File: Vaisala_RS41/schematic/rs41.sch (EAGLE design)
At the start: 268 parts, among them J201 SENSORBOOM, J601 expansion, J602 XDATA, Q201 BSS92, Q202 BSS92, Q203 BSS101, Q204 BSS101, Q501 E4JxA, Q502 BSS101, Q503 BSS101, Q601 BSS101, U101 STM32F100C8T6B, U201 TS3A4751, U202 TS5A9411, U203 TS5A9411, U204 TS5A9411, U205 74HCU04, U206 305G, U207 74LVC3G34, U208 NC7SZ27, U301 DIFFGEN, U302 UBX-6010MLF56, U303 SAW, U304 LNA, U401 SI4032QFN204X4, U501 TLV70030SOT23-5, U502 TPS61200, U503 TLV70030SOT23-5, U504 TLV70030SOT23-5, U601 25AA080SN, X101 24MHz, X301 tbd

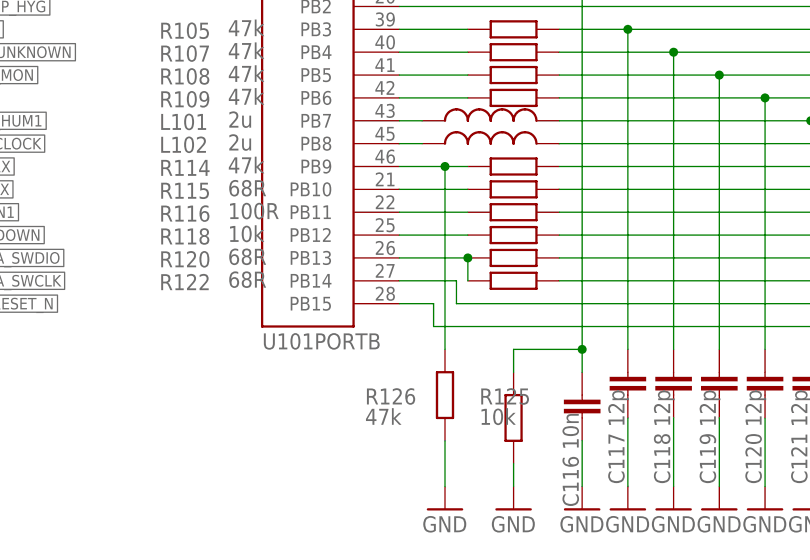
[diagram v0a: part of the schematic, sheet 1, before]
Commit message: R125 in RS41 sonde is connected to +3V, not GND, fixed
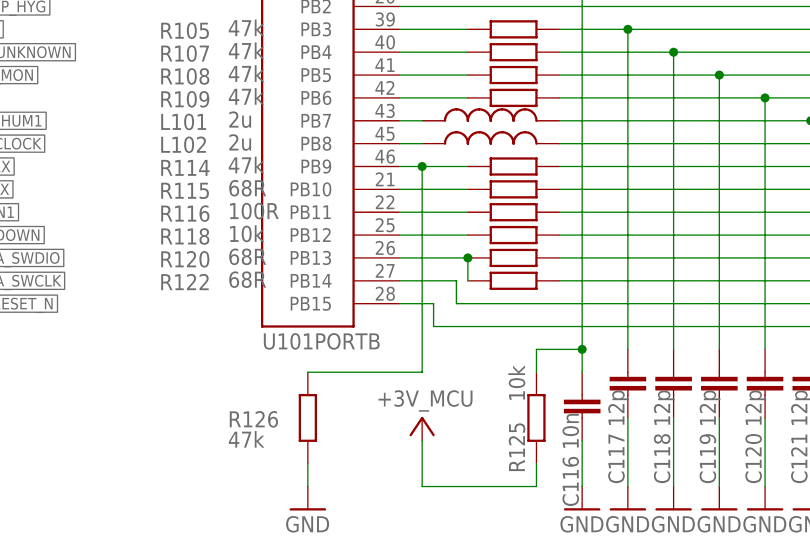
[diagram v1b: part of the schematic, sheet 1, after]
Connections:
- net +3V_MCU: now also R125.2
- net GND: no longer R125.2
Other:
- moved on the sheet: R125, R126
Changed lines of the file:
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@@
 <part name="GND4" library="supply1" library_urn="urn:adsk.eagle:library:371" deviceset="GND" device=""/>
 <part name="P+2" library="rs41" deviceset="+3V_ANA" device=""/>
-<part name="GND5" library="supply1" library_urn="urn:adsk.eagle:library:371" deviceset="GND" device=""/>
 <part name="F501" library="rs41" deviceset="FUSE" device="" value="tbd"/>
 <part name="GND6" library="supply1" library_urn="urn:adsk.eagle:library:371" deviceset="GND" device=""/>
@@
 <part name="P+11" library="rs41" deviceset="+3V_GPS" device=""/>
 <part name="GND20" library="supply1" library_urn="urn:adsk.eagle:library:371" deviceset="GND" device=""/>
+<part name="P+12" library="rs41" deviceset="+3V_MCU" device=""/>
 </parts>
 <sheets>
@@
 <attribute name="VALUE" x="-17.78" y="-20.32" size="1.778" layer="96"/>
 </instance>
-<instance part="R125" gate="G$1" x="66.04" y="-7.62" smashed="yes" rot="R270">
-<attribute name="NAME" x="62.23" y="-6.1214" size="1.778" layer="95"/>
-<attribute name="VALUE" x="62.23" y="-8.382" size="1.778" layer="96"/>
-</instance>
-<instance part="R126" gate="G$1" x="58.42" y="-5.08" smashed="yes" rot="R270">
-<attribute name="NAME" x="49.53" y="-6.1214" size="1.778" layer="95"/>
-<attribute name="VALUE" x="49.53" y="-8.382" size="1.778" layer="96"/>
+<instance part="R125" gate="G$1" x="68.58" y="-7.62" smashed="yes" rot="R270">
+<attribute name="NAME" x="67.31" y="-13.7414" size="1.778" layer="95" rot="R90"/>
+<attribute name="VALUE" x="67.31" y="-5.842" size="1.778" layer="96" rot="R90"/>
+</instance>
+<instance part="R126" gate="G$1" x="43.18" y="-7.62" smashed="yes" rot="R270">
+<attribute name="NAME" x="34.29" y="-8.6614" size="1.778" layer="95"/>
+<attribute name="VALUE" x="34.29" y="-10.922" size="1.778" layer="96"/>
 </instance>
 <instance part="C117" gate="G$1" x="78.74" y="-5.08" smashed="yes" rot="R180">
@@
 <attribute name="VALUE" x="34.29" y="6.858" size="1.778" layer="96"/>
 </instance>
-<instance part="GND114" gate="1" x="58.42" y="-17.78" smashed="yes">
-<attribute name="VALUE" x="55.88" y="-20.32" size="1.778" layer="96"/>
+<instance part="GND114" gate="1" x="43.18" y="-17.78" smashed="yes">
+<attribute name="VALUE" x="40.64" y="-20.32" size="1.778" layer="96"/>
 </instance>
 <instance part="GND115" gate="1" x="73.66" y="-17.78" smashed="yes">
@@
 <attribute name="VALUE" x="2.54" y="60.96" size="1.778" layer="96"/>
 </instance>
-<instance part="GND5" gate="1" x="66.04" y="-17.78" smashed="yes">
-<attribute name="VALUE" x="63.5" y="-20.32" size="1.778" layer="96"/>
-</instance>
 <instance part="L101" gate="G$1" x="63.5" y="25.4" smashed="yes" rot="R90">
 <attribute name="NAME" x="26.67" y="24.384" size="1.778" layer="95"/>
@@
 <attribute name="NAME" x="26.67" y="21.844" size="1.778" layer="95"/>
 <attribute name="VALUE" x="34.29" y="22.098" size="1.778" layer="96"/>
+</instance>
+<instance part="P+12" gate="G$1" x="55.88" y="-7.62" smashed="yes">
+<attribute name="VALUE" x="50.8" y="-6.35" size="1.778" layer="96"/>
 </instance>
 </instances>
@@
 <pinref part="GND114" gate="1" pin="GND"/>
 <pinref part="R126" gate="G$1" pin="2"/>
-<wire x1="58.42" y1="-10.16" x2="58.42" y2="-15.24" width="0.1524" layer="91"/>
+<wire x1="43.18" y1="-12.7" x2="43.18" y2="-15.24" width="0.1524" layer="91"/>
 </segment>
 <segment>
@@
 <pinref part="GND3" gate="1" pin="GND"/>
 </segment>
-<segment>
-<pinref part="R125" gate="G$1" pin="2"/>
-<pinref part="GND5" gate="1" pin="GND"/>
-<wire x1="66.04" y1="-15.24" x2="66.04" y2="-12.7" width="0.1524" layer="91"/>
-</segment>
 </net>
 <net name="N$106" class="0">
@@
 <pinref part="R114" gate="G$1" pin="2"/>
 <pinref part="U101" gate="PORTB" pin="PB9"/>
-<wire x1="60.96" y1="20.32" x2="58.42" y2="20.32" width="0.1524" layer="91"/>
+<wire x1="60.96" y1="20.32" x2="55.88" y2="20.32" width="0.1524" layer="91"/>
 <pinref part="R126" gate="G$1" pin="1"/>
-<wire x1="58.42" y1="20.32" x2="53.34" y2="20.32" width="0.1524" layer="91"/>
-<wire x1="58.42" y1="0" x2="58.42" y2="20.32" width="0.1524" layer="91"/>
-<junction x="58.42" y="20.32"/>
+<wire x1="55.88" y1="20.32" x2="53.34" y2="20.32" width="0.1524" layer="91"/>
+<wire x1="43.18" y1="-2.54" x2="55.88" y2="-2.54" width="0.1524" layer="91"/>
+<wire x1="55.88" y1="-2.54" x2="55.88" y2="20.32" width="0.1524" layer="91"/>
+<junction x="55.88" y="20.32"/>
 </segment>
 </net>
@@
 <pinref part="R125" gate="G$1" pin="1"/>
 <wire x1="73.66" y1="0" x2="73.66" y2="40.64" width="0.1524" layer="91"/>
-<wire x1="66.04" y1="-2.54" x2="66.04" y2="0" width="0.1524" layer="91"/>
-<wire x1="66.04" y1="0" x2="73.66" y2="0" width="0.1524" layer="91"/>
+<wire x1="68.58" y1="-2.54" x2="68.58" y2="0" width="0.1524" layer="91"/>
+<wire x1="68.58" y1="0" x2="73.66" y2="0" width="0.1524" layer="91"/>
 <junction x="73.66" y="0"/>
 </segment>
@@
 <pinref part="P+101" gate="G$1" pin="+3V_MCU"/>
 </segment>
-</net>
+<segment>
+<pinref part="P+12" gate="G$1" pin="+3V_MCU"/>
+<wire x1="55.88" y1="-10.16" x2="55.88" y2="-15.24" width="0.1524" layer="91"/>
+<pinref part="R125" gate="G$1" pin="2"/>
+<wire x1="68.58" y1="-15.24" x2="68.58" y2="-12.7" width="0.1524" layer="91"/>
+<wire x1="55.88" y1="-15.24" x2="68.58" y2="-15.24" width="0.1524" layer="91"/>
+</segment>
+</net>
